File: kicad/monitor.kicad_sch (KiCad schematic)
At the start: 5 parts, among them SW14 PH_IND

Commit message: layout updates
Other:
- note added: "direct monitor switch"
- note removed: "direct monitor knob"
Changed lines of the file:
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@@
 	(generator_version "10.0")
 	(paper "A4")
-	(text "direct monitor knob"
+	(text "direct monitor switch"
 		(exclude_from_sim no)
 		(at 213.106 175.006 0)

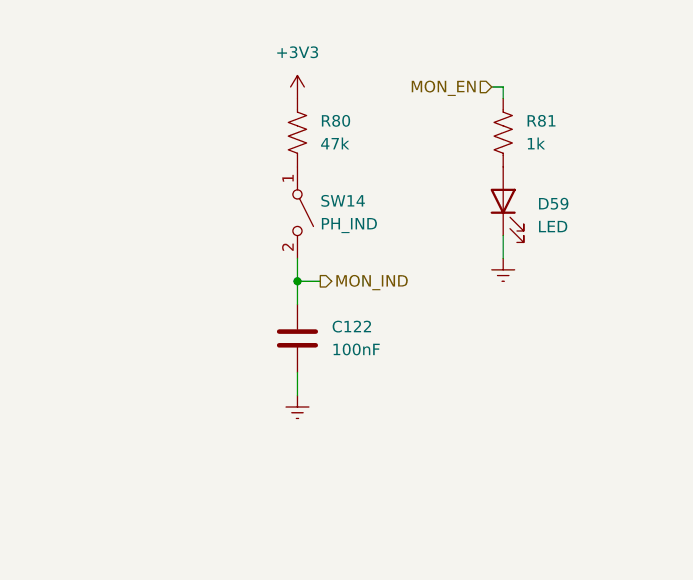
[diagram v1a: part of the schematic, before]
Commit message: push buttons
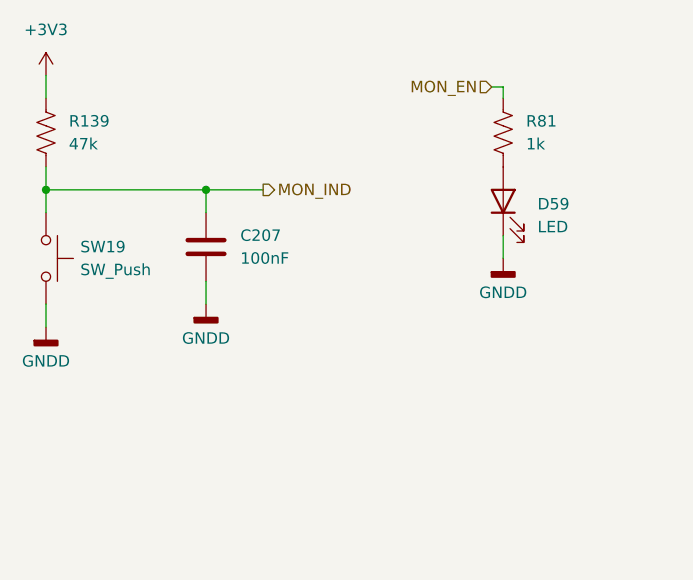
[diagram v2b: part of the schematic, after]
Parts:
- removed C122: 100nF, symbol Device:C
- removed R80: 47k, symbol Device:R_US
- removed SW14: PH_IND, symbol Switch:SW_SPST
- added C207: 100nF, Capacitor_SMD:C_0603_1608Metric_Pad1.08x0.95mm_HandSolder, symbol Device:C
- added R139: 47k, Resistor_SMD:R_0603_1608Metric_Pad0.98x0.95mm_HandSolder, symbol Device:R_US
- added SW19: SW_Push, Button_Switch_SMD:SW_Push_1P1T_XKB_TS-1187A, symbol Switch:SW_Push
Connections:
- net +3V3: now also R139.1
- net MON_IND: now also C207.1, R139.2, SW19.1
- net Earth renamed GNDD
- net GNDD: now also C207.2, SW19.2

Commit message: footprint selection
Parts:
- D59: footprint (none) -> LED_SMD:LED_0603_1608Metric_Pad1.05x0.95mm_HandSolder
- R81: footprint (none) -> Resistor_SMD:R_0603_1608Metric_Pad0.98x0.95mm_HandSolder
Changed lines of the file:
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@@
+			)
+		)
+		(property "KLC_S3.3" ""
+			(at 95.25 100.33 90)
+			(hide yes)
+			(show_name no)
+			(do_not_autoplace no)
+			(effects
+				(font
+					(size 1.27 1.27)
+				)
+			)
+		)
+		(property "KLC_S4.1" ""
+			(at 95.25 100.33 90)
+			(hide yes)
+			(show_name no)
+			(do_not_autoplace no)
+			(effects
+				(font
+					(size 1.27 1.27)
+				)
+			)
+		)
+		(property "Sim.Type" ""
+			(at 95.25 100.33 90)
+			(hide yes)
+			(show_name no)
+			(do_not_autoplace no)
+			(effects
+				(font
+					(size 1.27 1.27)
+				)
 			)
 		)
@@
 			)
 		)
+		(property "KLC_S3.3" ""
+			(at 113.03 99.06 0)
+			(hide yes)
+			(show_name no)
+			(do_not_autoplace no)
+			(effects
+				(font
+					(size 1.27 1.27)
+				)
+			)
+		)
+		(property "KLC_S4.1" ""
+			(at 113.03 99.06 0)
+			(hide yes)
+			(show_name no)
+			(do_not_autoplace no)
+			(effects
+				(font
+					(size 1.27 1.27)
+				)
+			)
+		)
+		(property "Sim.Type" ""
+			(at 113.03 99.06 0)
+			(hide yes)
+			(show_name no)
+			(do_not_autoplace no)
+			(effects
+				(font
+					(size 1.27 1.27)
+				)
+			)
+		)
 		(pin "1"
 		)
@@
 			)
 		)
-		(property "Footprint" ""
+		(property "Footprint" "Resistor_SMD:R_0603_1608Metric_Pad0.98x0.95mm_HandSolder"
 			(at 147.066 86.614 90)
 			(hide yes)
@@
 		)
 		(property "Description" "Resistor, US symbol"
+			(at 146.05 86.36 0)
+			(hide yes)
+			(show_name no)
+			(do_not_autoplace no)
+			(effects
+				(font
+					(size 1.27 1.27)
+				)
+			)
+		)
+		(property "KLC_S3.3" ""
+			(at 146.05 86.36 0)
+			(hide yes)
+			(show_name no)
+			(do_not_autoplace no)
+			(effects
+				(font
+					(size 1.27 1.27)
+				)
+			)
+		)
+		(property "KLC_S4.1" ""
+			(at 146.05 86.36 0)
+			(hide yes)
+			(show_name no)
+			(do_not_autoplace no)
+			(effects
+				(font
+					(size 1.27 1.27)
+				)
+			)
+		)
+		(property "Sim.Type" ""
 			(at 146.05 86.36 0)
 			(hide yes)
@@
 			)
 		)
+		(property "KLC_S3.3" ""
+			(at 95.25 86.36 0)
+			(hide yes)
+			(show_name no)
+			(do_not_autoplace no)
+			(effects
+				(font
+					(size 1.27 1.27)
+				)
+			)
+		)
+		(property "KLC_S4.1" ""
+			(at 95.25 86.36 0)
+			(hide yes)
+			(show_name no)
+			(do_not_autoplace no)
+			(effects
+				(font
+					(size 1.27 1.27)
+				)
+			)
+		)
+		(property "Sim.Type" ""
+			(at 95.25 86.36 0)
+			(hide yes)
+			(show_name no)
+			(do_not_autoplace no)
+			(effects
+				(font
+					(size 1.27 1.27)
+				)
+			)
+		)
 		(pin "1"
 		)
@@
 			)
 		)
-		(property "Footprint" ""
+		(property "Footprint" "LED_SMD:LED_0603_1608Metric_Pad1.05x0.95mm_HandSolder"
 			(at 146.05 93.98 0)
 			(hide yes)
@@
 			(hide yes)
 			(show_name no)
+			(do_not_autoplace no)
+			(effects
+				(font
+					(size 1.27 1.27)
+				)
+			)
+		)
+		(property "KLC_S3.3" ""
+			(at 146.05 93.98 90)
+			(hide yes)
+			(show_name no)
+			(do_not_autoplace no)
+			(effects
+				(font
+					(size 1.27 1.27)
+				)
+			)
+		)
+		(property "KLC_S4.1" ""
+			(at 146.05 93.98 90)
+			(hide yes)
+			(show_name no)
+			(do_not_autoplace no)
+			(effects
+				(font
+					(size 1.27 1.27)
+				)
+			)
+		)
+		(property "Sim.Type" ""
+			(at 146.05 93.98 90)
+			(hide yes)
+			(show_name no)

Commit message: output schematic pdfs
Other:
- note removed: "direct monitor switch"
- company: (none) -> OpenMic
- title: (none) -> Direct monitor switch
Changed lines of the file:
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@@
 	(generator "eeschema")
 	(generator_version "10.0")
-	(paper "A4")
-	(text "direct monitor switch"
-		(exclude_from_sim no)
-		(at 213.106 175.006 0)
-		(effects
-			(font
-				(size 2.54 2.54)
-			)
-			(justify left bottom)
-		)
+	(paper "USLetter")
+	(title_block
+		(title "Direct monitor switch")
+		(date "2026-05-15")
+		(company "OpenMic")
 	)
 	(junction
